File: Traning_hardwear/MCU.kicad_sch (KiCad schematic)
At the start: 2 parts, among them J1 RJ45_LED_Shielded, U1 Teensy4.1_DEV-16771

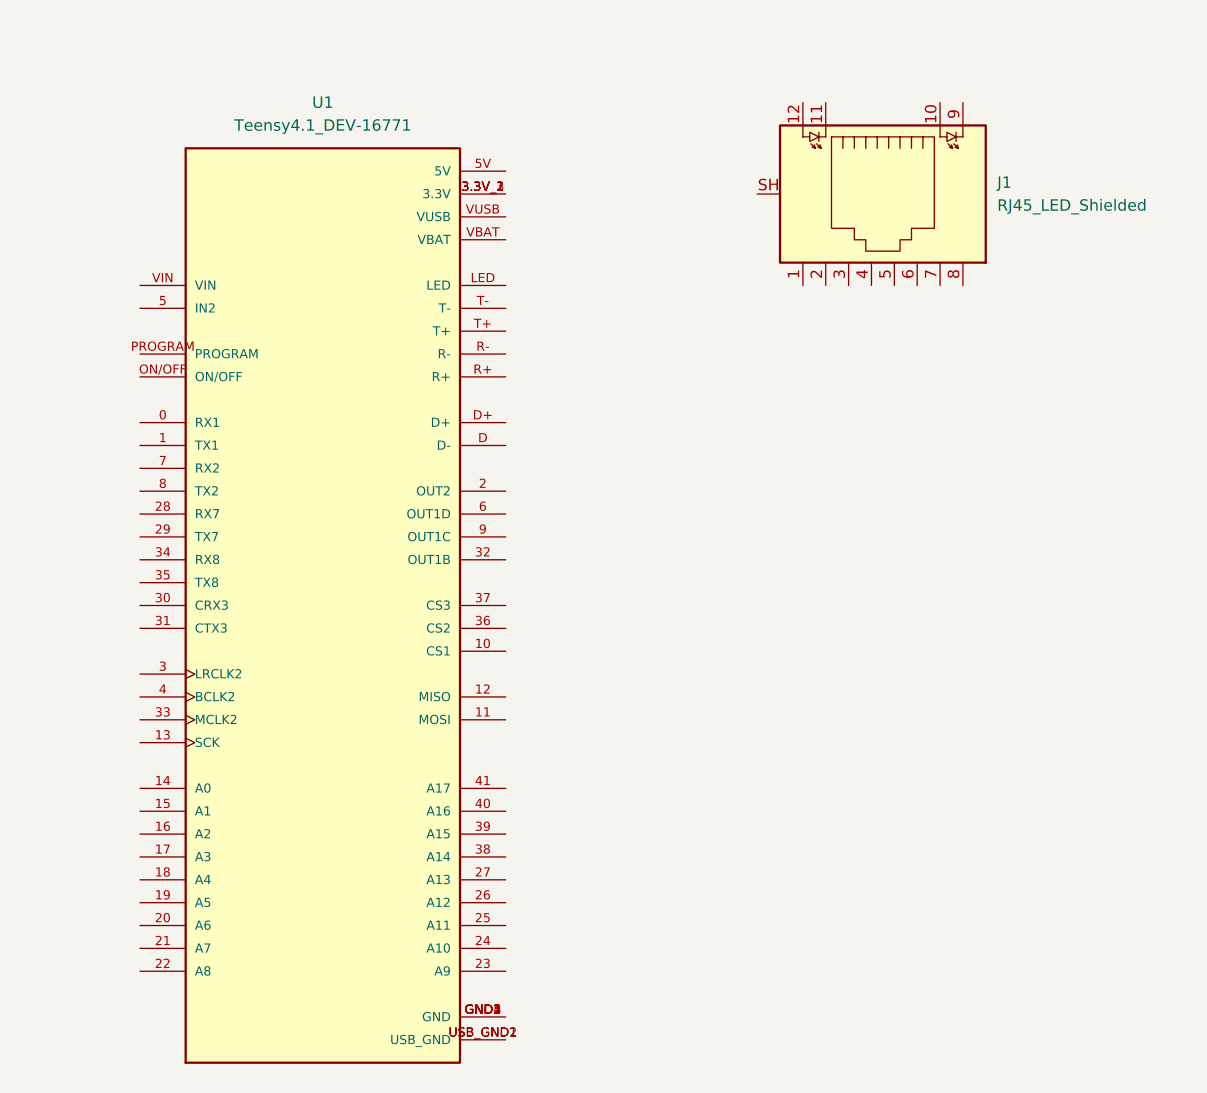
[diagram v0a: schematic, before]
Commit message: Add ethernet
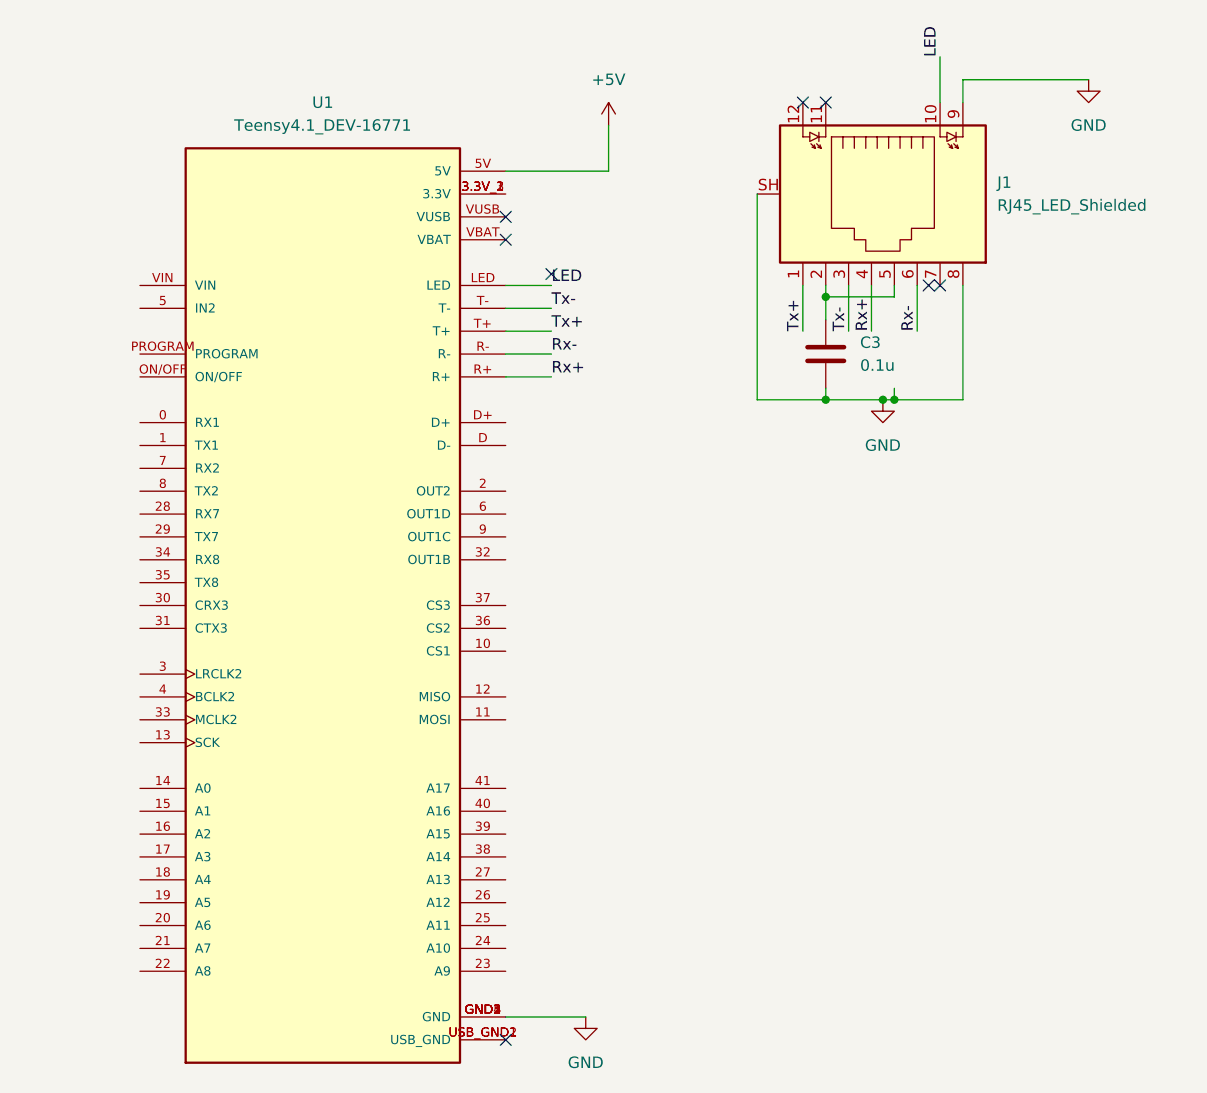
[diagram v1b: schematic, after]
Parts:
- added C3: 0.1u, symbol Device:C
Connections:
- net +5V: now reaches U1.5V
- net GND: now reaches U1.GND1 (GND), U1.GND2 (GND), U1.GND3 (GND), U1.GND4 (GND), U1.GND5 (GND)
- net GND: now also J1.8, J1.9, J1.SH, C3.2
- net LED: now reaches U1.LED
- net LED: now also J1.10
- net Rx+: now reaches U1.R+
- net Rx+: now also J1.4
- net Rx-: now reaches U1.R-
- net Rx-: now also J1.6
- net Tx+: now reaches U1.T+
- net Tx+: now also J1.1
- net Tx-: now reaches U1.T-
- net Tx-: now also J1.3
- net at J1.2: now also J1.5, C3.1
- no-connect marks 0 -> 8

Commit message: Finish Schematic
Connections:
- net STBY: now reaches U1.2 (OUT2)
- net CTX1: now reaches U1.22 (A8)
- net CRX1: now reaches U1.23 (A9)
- net +3V3: now reaches U1.3.3V_1 (3.3V), U1.3.3V_2 (3.3V), U1.3.3V_3 (3.3V)
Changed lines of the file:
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@@
+	(wire
+		(pts
+			(xy 152.4 135.89) (xy 157.48 135.89)
+		)
+		(stroke
+			(width 0)
+			(type default)
+		)
+	)
+	(wire
+		(pts
+			(xy 152.4 49.53) (xy 168.91 49.53)
+		)
+		(stroke
+			(width 0)
+			(type default)
+		)
+	)
+	(wire
+		(pts
+			(xy 168.91 44.45) (xy 168.91 49.53)
+		)
+		(stroke
+			(width 0)
+			(type default)
+		)
+	)
 	(wire
 		(pts
@@
 		(pts
 			(xy 203.2 59.69) (xy 203.2 72.39)
+		)
+		(stroke
+			(width 0)
+			(type default)
+		)
+	)
+	(wire
+		(pts
+			(xy 105.41 135.89) (xy 111.76 135.89)
+		)
+		(stroke
+			(width 0)
+			(type default)
+		)
+	)
+	(wire
+		(pts
+			(xy 152.4 82.55) (xy 157.48 82.55)
 		)
 		(stroke
@@
 			)
 			(justify left bottom)
+		)
+	)
+	(hierarchical_label "CRX1"
+		(shape input)
+		(at 157.48 135.89 0)
+		(effects
+			(font
+				(size 1.27 1.27)
+			)
+			(justify left)
+		)
+	)
+	(hierarchical_label "STBY"
+		(shape output)
+		(at 157.48 82.55 0)
+		(effects
+			(font
+				(size 1.27 1.27)
+			)
+			(justify left)
+		)
+	)
+	(hierarchical_label "CTX1"
+		(shape output)
+		(at 105.41 135.89 180)
+		(effects
+			(font
+				(size 1.27 1.27)
+			)
+			(justify right)
 		)
 	)
@@
 					(unit 1)
 				)
+			)
+		)
+	)
+	(symbol
+		(lib_id "power:+3V3")
+		(at 168.91 44.45 0)
+		(unit 1)
+		(exclude_from_sim no)
+		(in_bom yes)
+		(on_board yes)
+		(dnp no)
+		(fields_autoplaced yes)
+		(property "Reference" "#PWR015"
+			(at 168.91 48.26 0)
+			(effects
+				(font
+					(size 1.27 1.27)
+				)
+				(hide yes)
+			)
+		)
+		(property "Value" "+3V3"
+			(at 168.91 39.37 0)
+			(effects
+				(font
+					(size 1.27 1.27)
+				)
+			)
+		)
+		(property "Footprint" ""
+			(at 168.91 44.45 0)
+			(effects
+				(font
+					(size 1.27 1.27)
+				)
+				(hide yes)
+			)
+		)
+		(property "Datasheet" ""
+			(at 168.91 44.45 0)
+			(effects
+				(font
+					(size 1.27 1.27)
+				)
+				(hide yes)
+			)
+		)
+		(property "Description" "Power symbol creates a global label with name \"+3V3\""
+			(at 168.91 44.45 0)
+			(effects
+				(font
+					(size 1.27 1.27)
+				)
+				(hide yes)
+			)
+		)
+		(pin "1"
+		)
+		(instances
+			(project ""
+				(path "/30fb269d-181e-4844-9e82-e5c3e09101dc/89da37a1-4554-47b7-9548-278a94db0d8e"
+					(reference "#PWR015")
+					(unit 1)
+				)
